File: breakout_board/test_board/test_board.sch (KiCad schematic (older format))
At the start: 12 parts, among them P1 CONN_01X05, P2 CONN_01X02, P3 CONN_01X25, P4 CONN_01X04, P5 CONN_01X02, P6 CONN_01X04

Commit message: pcb: minor changes
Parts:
- added P7: CONN_01X02, symbol CONN_01X02
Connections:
- net GND: now also P7.1 (P1)
- net VDD: now also P7.2 (P2)
- no-connect marks 0 -> 6
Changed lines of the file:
@@
 $EndComp
 $Comp
-L Earth #PWR4
+L Earth #PWR01
 U 1 1 56ED4F6D
 P 6700 2650
-F 0 "#PWR4" H 6700 2400 50  0001 C CNN
+F 0 "#PWR01" H 6700 2400 50  0001 C CNN
 F 1 "Earth" H 6700 2500 50  0001 C CNN
 F 2 "" H 6700 2650 50  0000 C CNN
@@
 $EndComp
 $Comp
-L Earth #PWR9
+L Earth #PWR02
 U 1 1 56ED53FB
-P 7750 5050
-F 0 "#PWR9" H 7750 4800 50  0001 C CNN
-F 1 "Earth" H 7750 4900 50  0001 C CNN
-F 2 "" H 7750 5050 50  0000 C CNN
-F 3 "" H 7750 5050 50  0000 C CNN
-	1    7750 5050
-	0    1    1    0
-$EndComp
-Text Label 8550 5050 2    60   ~ 0
+P 7350 5050
+F 0 "#PWR02" H 7350 4800 50  0001 C CNN
+F 1 "Earth" H 7350 4900 50  0001 C CNN
+F 2 "" H 7350 5050 50  0000 C CNN
+F 3 "" H 7350 5050 50  0000 C CNN
+	1    7350 5050
+	0    1    1    0
+$EndComp
+Text Label 7750 5050 2    60   ~ 0
 ESD
 Text Label 8400 2750 0    60   ~ 0
@@
 	8100 2650 6700 2650
 Wire Wire Line
-	7750 5050 8100 5050
+	7350 5050 8100 5050
 Text Label 8400 3150 0    60   ~ 0
 VDD
@@
 Connection ~ 5950 3350
 $Comp
-L Earth #PWR3
+L Earth #PWR03
 U 1 1 56ED6FD4
 P 5800 3750
-F 0 "#PWR3" H 5800 3500 50  0001 C CNN
+F 0 "#PWR03" H 5800 3500 50  0001 C CNN
 F 1 "Earth" H 5800 3600 50  0001 C CNN
 F 2 "" H 5800 3750 50  0000 C CNN
@@
 	8100 3950 7750 3950
 $Comp
-L GND #PWR7
+L GND #PWR04
 U 1 1 56ED8B2B
 P 7750 3950
-F 0 "#PWR7" H 7750 3700 50  0001 C CNN
+F 0 "#PWR04" H 7750 3700 50  0001 C CNN
 F 1 "GND" H 7750 3800 50  0000 C CNN
 F 2 "" H 7750 3950 50  0000 C CNN
@@
 	8100 4850 7750 4850
 $Comp
-L GND #PWR8
+L GND #PWR05
 U 1 1 56ED8D65
 P 7750 4850
-F 0 "#PWR8" H 7750 4600 50  0001 C CNN
+F 0 "#PWR05" H 7750 4600 50  0001 C CNN
 F 1 "GND" H 7750 4700 50  0000 C CNN
 F 2 "" H 7750 4850 50  0000 C CNN
@@
 SDA
 $Comp
-L GND #PWR6
+L GND #PWR06
 U 1 1 56ED96BD
 P 7750 3700
-F 0 "#PWR6" H 7750 3450 50  0001 C CNN
+F 0 "#PWR06" H 7750 3450 50  0001 C CNN
 F 1 "GND" H 7750 3550 50  0000 C CNN
 F 2 "" H 7750 3700 50  0000 C CNN
@@
 	7000 3350 8100 3350
 $Comp
-L Earth #PWR5
+L Earth #PWR07
 U 1 1 56ED9873
 P 7000 3750
-F 0 "#PWR5" H 7000 3500 50  0001 C CNN
+F 0 "#PWR07" H 7000 3500 50  0001 C CNN
 F 1 "Earth" H 7000 3600 50  0001 C CNN
 F 2 "" H 7000 3750 50  0000 C CNN
@@
 	5750 3350 6350 3350
 $Comp
-L VDD #PWR2
+L VDD #PWR08
 U 1 1 56ED9A6A
 P 5750 3350
-F 0 "#PWR2" H 5750 3200 50  0001 C CNN
+F 0 "#PWR08" H 5750 3200 50  0001 C CNN
 F 1 "VDD" H 5750 3500 50  0000 C CNN
 F 2 "" H 5750 3350 50  0000 C CNN
@@
 	6250 3250 5350 3250
 $Comp
-L Earth #PWR1
+L Earth #PWR09
 U 1 1 56EDA160
 P 4750 3050
-F 0 "#PWR1" H 4750 2800 50  0001 C CNN
+F 0 "#PWR09" H 4750 2800 50  0001 C CNN
 F 1 "Earth" H 4750 2900 50  0001 C CNN
 F 2 "" H 4750 3050 50  0000 C CNN
@@
 Text Label 6650 5600 0    60   ~ 0
 YU
+$Comp
+L CONN_01X02 P7
+U 1 1 56EDDFD4
+P 4100 3600
+F 0 "P7" H 4100 3750 50  0000 C CNN
+F 1 "CONN_01X02" V 4200 3600 50  0000 C CNN
+F 2 "" H 4100 3600 50  0000 C CNN
+F 3 "" H 4100 3600 50  0000 C CNN
+	1    4100 3600
+	-1   0    0    1
+$EndComp
+Wire Wire Line
+	4300 3550 4550 3550
+Wire Wire Line
+	4300 3650 4550 3650
+Text Label 4550 3550 0    60   ~ 0
+VDD
+Text Label 4550 3650 0    60   ~ 0
+GND
+NoConn ~ 8100 4050
+NoConn ~ 8100 4150
+NoConn ~ 8100 4250
+NoConn ~ 8100 4350
+NoConn ~ 8100 4450
+NoConn ~ 8100 4550
+$Comp
+L PWR_FLAG #FLG010
+U 1 1 56EDE7CF
+P 5650 4350
+F 0 "#FLG010" H 5650 4445 50  0001 C CNN
+F 1 "PWR_FLAG" H 5650 4530 50  0000 C CNN
+F 2 "" H 5650 4350 50  0000 C CNN
+F 3 "" H 5650 4350 50  0000 C CNN
+	1    5650 4350
+	1    0    0    -1
+$EndComp
+$Comp
+L PWR_FLAG #FLG011
+U 1 1 56EDE7FD
+P 6250 4350
+F 0 "#FLG011" H 6250 4445 50  0001 C CNN
+F 1 "PWR_FLAG" H 6250 4530 50  0000 C CNN
+F 2 "" H 6250 4350 50  0000 C CNN
+F 3 "" H 6250 4350 50  0000 C CNN
+	1    6250 4350
+	1    0    0    -1
+$EndComp
+$Comp
+L GND #PWR012
+U 1 1 56EDE82B
+P 6250 4350
+F 0 "#PWR012" H 6250 4100 50  0001 C CNN
+F 1 "GND" H 6250 4200 50  0000 C CNN
+F 2 "" H 6250 4350 50  0000 C CNN
+F 3 "" H 6250 4350 50  0000 C CNN
+	1    6250 4350
+	1    0    0    -1
+$EndComp
+$Comp
+L VDD #PWR013
+U 1 1 56EDE859
+P 5650 4350
+F 0 "#PWR013" H 5650 4200 50  0001 C CNN
+F 1 "VDD" H 5650 4500 50  0000 C CNN
+F 2 "" H 5650 4350 50  0000 C CNN
+F 3 "" H 5650 4350 50  0000 C CNN
+	1    5650 4350
+	-1   0    0    1
+$EndComp
 $EndSCHEMATC

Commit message: pcb: added footprint for the capacitors
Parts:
- C1: footprint (none) -> Capacitors_SMD:C_0603_HandSoldering
- C2, C3, C4, C5: footprint (none) -> Capacitors_SMD:C_1206_HandSoldering
- C6: footprint (none) -> Capacitors_SMD:C_0402
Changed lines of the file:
@@
 LIBS:contrib
 LIBS:valves
+LIBS:test_board-cache
 EELAYER 25 0
 EELAYER END
@@
 F 0 "P3" H 8300 5150 50  0000 C CNN
 F 1 "CONN_01X25" V 8400 3850 50  0000 C CNN
-F 2 "" H 8300 3850 50  0000 C CNN
+F 2 "" H 8300 3850 50  0001 C CNN
 F 3 "" H 8300 3850 50  0000 C CNN
 	1    8300 3850
@@
 F 0 "P4" H 8300 5700 50  0000 C CNN
 F 1 "CONN_01X04" V 8400 5450 50  0000 C CNN
-F 2 "" H 8300 5450 50  0000 C CNN
+F 2 "" H 8300 5450 50  0001 C CNN
 F 3 "" H 8300 5450 50  0000 C CNN
 	1    8300 5450
@@
 F 0 "P2" H 8250 2350 50  0000 C CNN
 F 1 "CONN_01X02" V 8350 2200 50  0000 C CNN
-F 2 "" H 8250 2200 50  0000 C CNN
+F 2 "" H 8250 2200 50  0001 C CNN
 F 3 "" H 8250 2200 50  0000 C CNN
 	1    8250 2200
@@
 F 0 "P1" H 4100 4600 50  0000 C CNN
 F 1 "CONN_01X05" V 4200 4300 50  0000 C CNN
-F 2 "" H 4100 4300 50  0000 C CNN
+F 2 "" H 4100 4300 50  0001 C CNN
 F 3 "" H 4100 4300 50  0000 C CNN
 	1    4100 4300
@@
 F 0 "C4" H 5975 3100 50  0000 L CNN
 F 1 "1uF" H 5975 2900 50  0000 L CNN
-F 2 "" H 5988 2850 50  0000 C CNN
+F 2 "Capacitors_SMD:C_1206_HandSoldering" H 5988 2850 50  0001 C CNN
 F 3 "" H 5950 3000 50  0000 C CNN
 	1    5950 3000
@@
 F 0 "C5" H 7025 3600 50  0000 L CNN
 F 1 "1uF" H 7025 3400 50  0000 L CNN
-F 2 "" H 7038 3350 50  0000 C CNN
+F 2 "Capacitors_SMD:C_1206_HandSoldering" H 7038 3350 50  0001 C CNN
 F 3 "" H 7000 3500 50  0000 C CNN
 	1    7000 3500
@@
 F 0 "C2" H 5125 2950 50  0000 L CNN
 F 1 "1uF" H 5125 2750 50  0000 L CNN
-F 2 "" H 5138 2700 50  0000 C CNN
+F 2 "Capacitors_SMD:C_1206_HandSoldering" H 5138 2700 50  0001 C CNN
 F 3 "" H 5100 2850 50  0000 C CNN
 	1    5100 2850
@@
 F 0 "C3" H 5225 3350 50  0000 L CNN
 F 1 "1uF" H 5225 3150 50  0000 L CNN
-F 2 "" H 5238 3100 50  0000 C CNN
+F 2 "Capacitors_SMD:C_1206_HandSoldering" H 5238 3100 50  0001 C CNN
 F 3 "" H 5200 3250 50  0000 C CNN
 	1    5200 3250
@@
 F 0 "C1" H 5975 3650 50  0000 L CNN
 F 1 "10uF" H 5975 3450 50  0000 L CNN
-F 2 "" H 5950 3550 50  0000 C CNN
+F 2 "Capacitors_SMD:C_0603_HandSoldering" H 5950 3550 50  0001 C CNN
 F 3 "" H 5950 3550 50  0000 C CNN
 	1    5950 3550
@@
 F 0 "C6" H 6225 3650 50  0000 L CNN
 F 1 "0.1uF" H 6225 3450 50  0000 L CNN
-F 2 "" H 6238 3400 50  0000 C CNN
+F 2 "Capacitors_SMD:C_0402" H 6238 3400 50  0001 C CNN
 F 3 "" H 6200 3550 50  0000 C CNN
 	1    6200 3550
@@
 F 0 "P5" H 4050 2350 50  0000 C CNN
 F 1 "CONN_01X02" V 4150 2200 50  0000 C CNN
-F 2 "" H 4050 2200 50  0000 C CNN
+F 2 "" H 4050 2200 50  0001 C CNN
 F 3 "" H 4050 2200 50  0000 C CNN
 	1    4050 2200
@@
 F 0 "P6" H 4100 5700 50  0000 C CNN
 F 1 "CONN_01X04" V 4200 5450 50  0000 C CNN
-F 2 "" H 4100 5450 50  0000 C CNN
+F 2 "" H 4100 5450 50  0001 C CNN
 F 3 "" H 4100 5450 50  0000 C CNN
 	1    4100 5450
@@
 F 0 "P7" H 4100 3750 50  0000 C CNN
 F 1 "CONN_01X02" V 4200 3600 50  0000 C CNN
-F 2 "" H 4100 3600 50  0000 C CNN
+F 2 "" H 4100 3600 50  0001 C CNN
 F 3 "" H 4100 3600 50  0000 C CNN
 	1    4100 3600

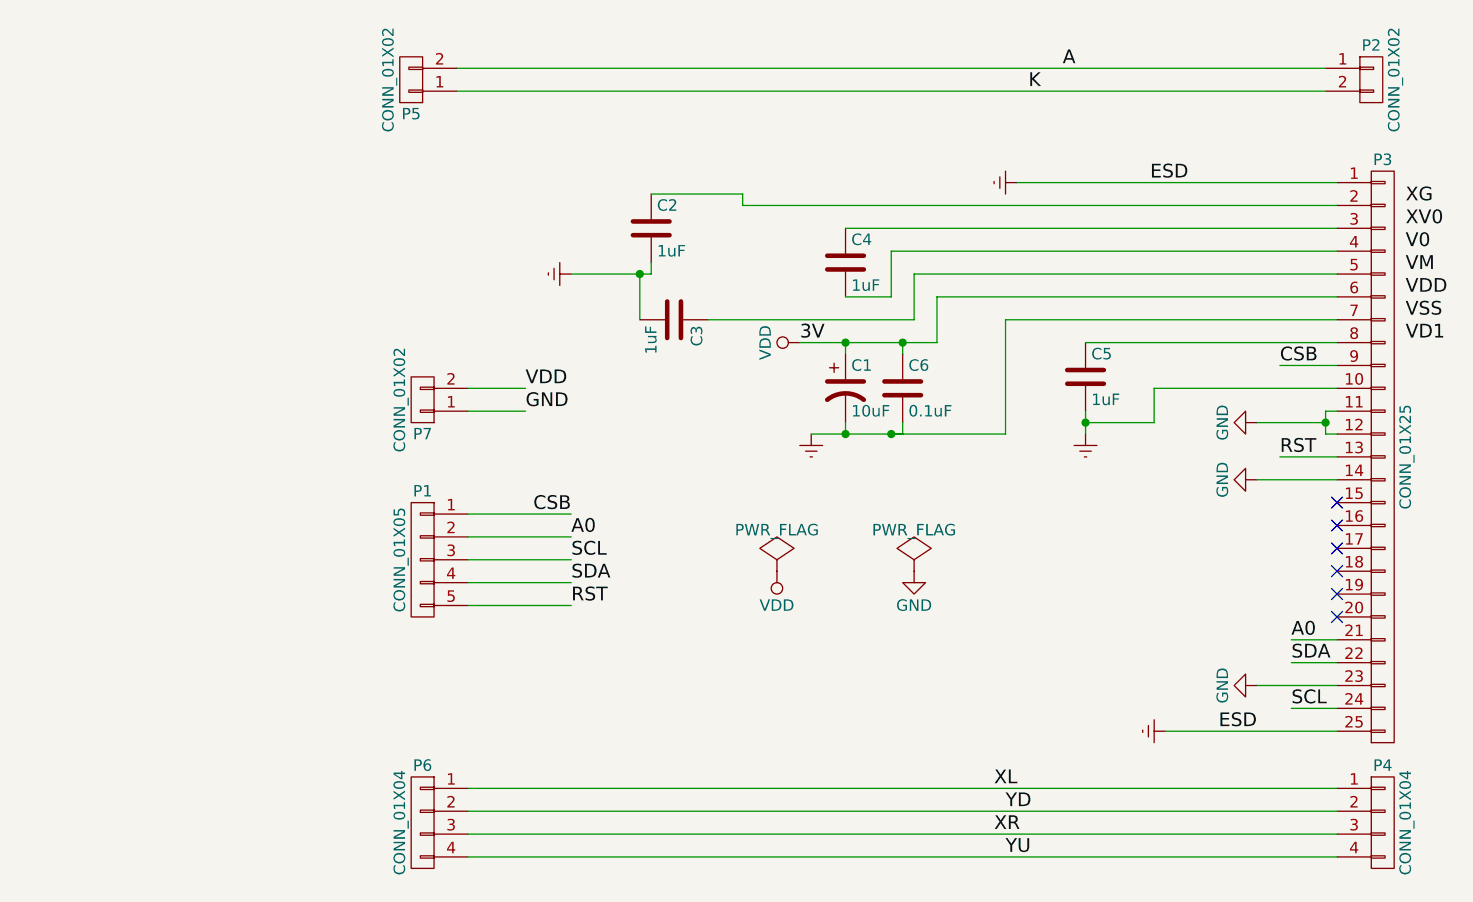
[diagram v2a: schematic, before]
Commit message: pcb: added all the footprints
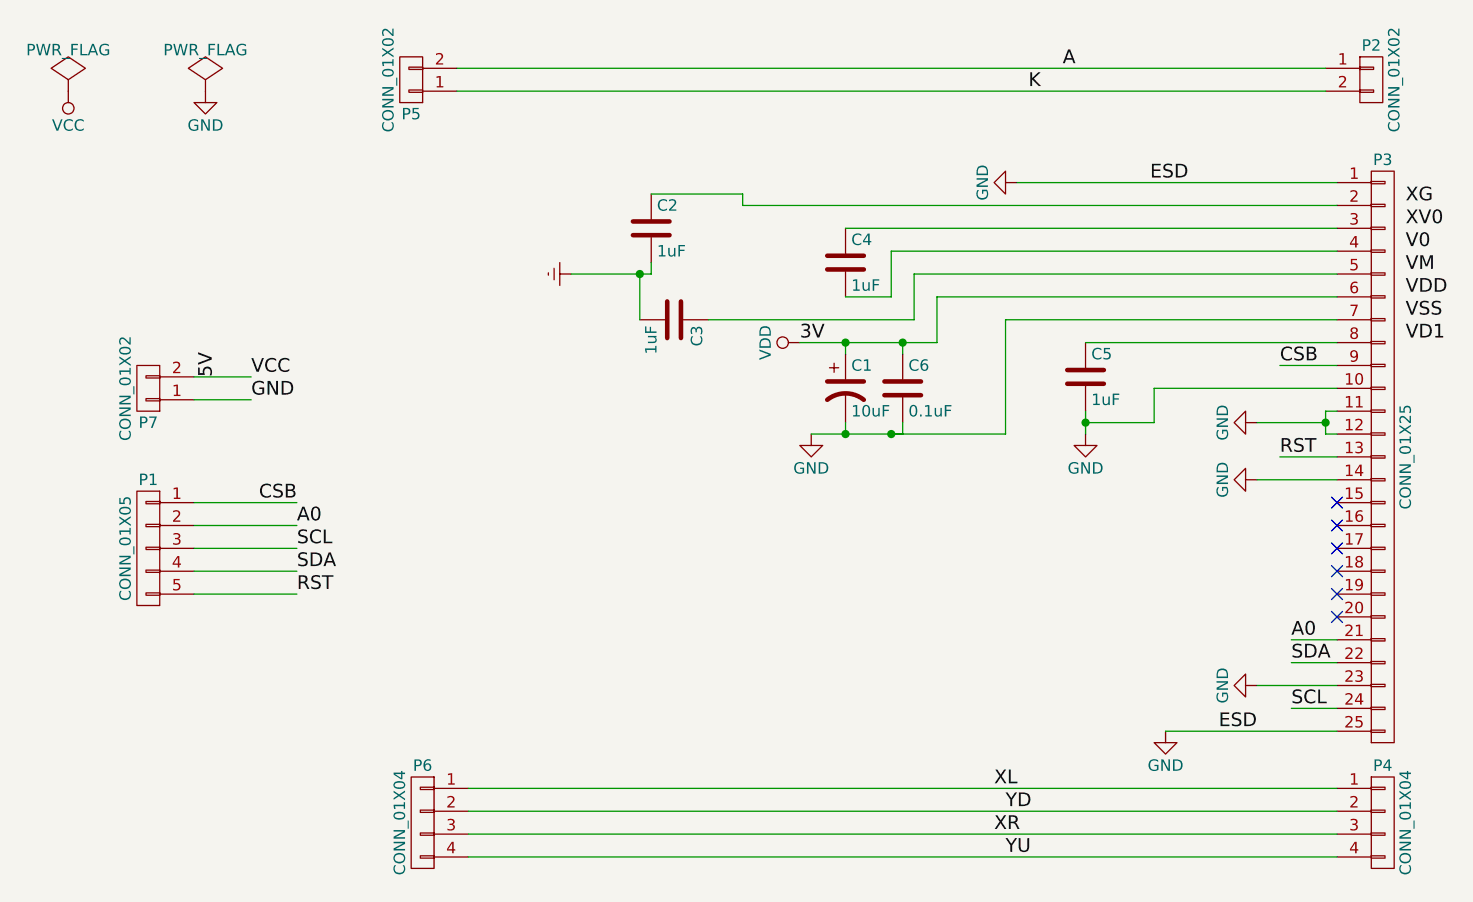
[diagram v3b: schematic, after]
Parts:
- P1: footprint (none) -> Socket_Strips:Socket_Strip_Straight_1x05
- P2, P5, P7: footprint (none) -> MyFootprints:Molex_kk_22_2_2021
- P3: footprint (none) -> MyFootprints:fpc_lcd
- P4: footprint (none) -> MyFootprints:SLW4S-1C7LF
- P6: footprint (none) -> Socket_Strips:Socket_Strip_Straight_1x04
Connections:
- net Earth: no longer C1.2, C5.2, C6.2, P3.1 (P1), P3.10 (P10), P3.25 (P25), P3.7 (P7)
- net GND: now also C1.2, C5.2, C6.2, P3.1 (P1), P3.10 (P10), P3.25 (P25), P3.7 (P7)
- net VDD: no longer P7.2 (P2)
- new net VCC: P7.2 (P2)
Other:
- moved on the sheet: P1, P7
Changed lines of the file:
@@
 F 0 "P3" H 8300 5150 50  0000 C CNN
 F 1 "CONN_01X25" V 8400 3850 50  0000 C CNN
-F 2 "" H 8300 3850 50  0001 C CNN
+F 2 "MyFootprints:fpc_lcd" H 8300 3850 50  0001 C CNN
 F 3 "" H 8300 3850 50  0000 C CNN
 	1    8300 3850
@@
 F 0 "P4" H 8300 5700 50  0000 C CNN
 F 1 "CONN_01X04" V 8400 5450 50  0000 C CNN
-F 2 "" H 8300 5450 50  0001 C CNN
+F 2 "MyFootprints:SLW4S-1C7LF" H 8300 5450 50  0001 C CNN
 F 3 "" H 8300 5450 50  0000 C CNN
 	1    8300 5450
@@
 F 0 "P2" H 8250 2350 50  0000 C CNN
 F 1 "CONN_01X02" V 8350 2200 50  0000 C CNN
-F 2 "" H 8250 2200 50  0001 C CNN
+F 2 "MyFootprints:Molex_kk_22_2_2021" H 8250 2200 50  0001 C CNN
 F 3 "" H 8250 2200 50  0000 C CNN
 	1    8250 2200
@@
 L CONN_01X05 P1
 U 1 1 56ED3F33
-P 4100 4300
-F 0 "P1" H 4100 4600 50  0000 C CNN
-F 1 "CONN_01X05" V 4200 4300 50  0000 C CNN
-F 2 "" H 4100 4300 50  0001 C CNN
-F 3 "" H 4100 4300 50  0000 C CNN
-	1    4100 4300
+P 2900 4250
+F 0 "P1" H 2900 4550 50  0000 C CNN
+F 1 "CONN_01X05" V 3000 4250 50  0000 C CNN
+F 2 "Socket_Strips:Socket_Strip_Straight_1x05" H 2900 4250 50  0001 C CNN
+F 3 "" H 2900 4250 50  0000 C CNN
+	1    2900 4250
 	-1   0    0    -1
 $EndComp
@@
 	1    5950 3550
 	1    0    0    -1
-$EndComp
-$Comp
-L Earth #PWR01
-U 1 1 56ED4F6D
-P 6700 2650
-F 0 "#PWR01" H 6700 2400 50  0001 C CNN
-F 1 "Earth" H 6700 2500 50  0001 C CNN
-F 2 "" H 6700 2650 50  0000 C CNN
-F 3 "" H 6700 2650 50  0000 C CNN
-	1    6700 2650
-	0    1    1    0
-$EndComp
-$Comp
-L Earth #PWR02
-U 1 1 56ED53FB
-P 7350 5050
-F 0 "#PWR02" H 7350 4800 50  0001 C CNN
-F 1 "Earth" H 7350 4900 50  0001 C CNN
-F 2 "" H 7350 5050 50  0000 C CNN
-F 3 "" H 7350 5050 50  0000 C CNN
-	1    7350 5050
-	0    1    1    0
 $EndComp
 Text Label 7750 5050 2    60   ~ 0
@@
 	5950 3400 5950 3350
 Connection ~ 5950 3350
-$Comp
-L Earth #PWR03
-U 1 1 56ED6FD4
-P 5800 3750
-F 0 "#PWR03" H 5800 3500 50  0001 C CNN
-F 1 "Earth" H 5800 3600 50  0001 C CNN
-F 2 "" H 5800 3750 50  0000 C CNN
-F 3 "" H 5800 3750 50  0000 C CNN
-	1    5800 3750
-	1    0    0    -1
-$EndComp
 Wire Wire Line
 	6200 3750 6200 3700
@@
 ESD
 Wire Wire Line
-	4300 4100 4750 4100
-Text Label 4750 4100 2    60   ~ 0
+	3100 4050 3550 4050
+Text Label 3550 4050 2    60   ~ 0
 CSB
 Wire Wire Line
@@
 CSB
 Wire Wire Line
-	4300 4500 4750 4500
-Wire Wire Line
-	4300 4400 4750 4400
-Wire Wire Line
-	4300 4300 4750 4300
-Wire Wire Line
-	4300 4200 4750 4200
-Text Label 4750 4500 0    60   ~ 0
+	3100 4450 3550 4450
+Wire Wire Line
+	3100 4350 3550 4350
+Wire Wire Line
+	3100 4250 3550 4250
+Wire Wire Line
+	3100 4150 3550 4150
+Text Label 3550 4450 0    60   ~ 0
 RST
 Wire Wire Line
@@
 	8100 3950 7750 3950
 $Comp
-L GND #PWR04
+L GND #PWR01
 U 1 1 56ED8B2B
 P 7750 3950
-F 0 "#PWR04" H 7750 3700 50  0001 C CNN
+F 0 "#PWR01" H 7750 3700 50  0001 C CNN
 F 1 "GND" H 7750 3800 50  0000 C CNN
 F 2 "" H 7750 3950 50  0000 C CNN
@@
 	8100 4850 7750 4850
 $Comp
-L GND #PWR05
+L GND #PWR02
 U 1 1 56ED8D65
 P 7750 4850
-F 0 "#PWR05" H 7750 4600 50  0001 C CNN
+F 0 "#PWR02" H 7750 4600 50  0001 C CNN
 F 1 "GND" H 7750 4700 50  0000 C CNN
 F 2 "" H 7750 4850 50  0000 C CNN
@@
 Text Label 7900 4950 0    60   ~ 0
 SCL
-Text Label 4750 4200 0    60   ~ 0
+Text Label 3550 4150 0    60   ~ 0
 A0
-Text Label 4750 4300 0    60   ~ 0
+Text Label 3550 4250 0    60   ~ 0
 SCL
-Text Label 4750 4400 0    60   ~ 0
+Text Label 3550 4350 0    60   ~ 0
 SDA
 $Comp
-L GND #PWR06
+L GND #PWR03
 U 1 1 56ED96BD
 P 7750 3700
-F 0 "#PWR06" H 7750 3450 50  0001 C CNN
+F 0 "#PWR03" H 7750 3450 50  0001 C CNN
 F 1 "GND" H 7750 3550 50  0000 C CNN
 F 2 "" H 7750 3700 50  0000 C CNN
@@
 Wire Wire Line
 	7000 3350 8100 3350
-$Comp
-L Earth #PWR07
-U 1 1 56ED9873
-P 7000 3750
-F 0 "#PWR07" H 7000 3500 50  0001 C CNN
-F 1 "Earth" H 7000 3600 50  0001 C CNN
-F 2 "" H 7000 3750 50  0000 C CNN
-F 3 "" H 7000 3750 50  0000 C CNN
-	1    7000 3750
-	1    0    0    -1
-$EndComp
 Wire Wire Line
 	7000 3650 7000 3750
@@
 	5750 3350 6350 3350
 $Comp
-L VDD #PWR08
+L VDD #PWR04
 U 1 1 56ED9A6A
 P 5750 3350
-F 0 "#PWR08" H 5750 3200 50  0001 C CNN
+F 0 "#PWR04" H 5750 3200 50  0001 C CNN
 F 1 "VDD" H 5750 3500 50  0000 C CNN
 F 2 "" H 5750 3350 50  0000 C CNN
@@
 	6250 3250 5350 3250
 $Comp
-L Earth #PWR09
+L Earth #PWR05
 U 1 1 56EDA160
 P 4750 3050
-F 0 "#PWR09" H 4750 2800 50  0001 C CNN
+F 0 "#PWR05" H 4750 2800 50  0001 C CNN
 F 1 "Earth" H 4750 2900 50  0001 C CNN
 F 2 "" H 4750 3050 50  0000 C CNN
@@
 F 0 "P5" H 4050 2350 50  0000 C CNN
 F 1 "CONN_01X02" V 4150 2200 50  0000 C CNN
-F 2 "" H 4050 2200 50  0001 C CNN
+F 2 "MyFootprints:Molex_kk_22_2_2021" H 4050 2200 50  0001 C CNN
 F 3 "" H 4050 2200 50  0000 C CNN
 	1    4050 2200
@@
 F 0 "P6" H 4100 5700 50  0000 C CNN
 F 1 "CONN_01X04" V 4200 5450 50  0000 C CNN
-F 2 "" H 4100 5450 50  0001 C CNN
+F 2 "Socket_Strips:Socket_Strip_Straight_1x04" H 4100 5450 50  0001 C CNN
 F 3 "" H 4100 5450 50  0000 C CNN
 	1    4100 5450
@@
 L CONN_01X02 P7
 U 1 1 56EDDFD4
-P 4100 3600
-F 0 "P7" H 4100 3750 50  0000 C CNN
-F 1 "CONN_01X02" V 4200 3600 50  0000 C CNN
-F 2 "" H 4100 3600 50  0001 C CNN
-F 3 "" H 4100 3600 50  0000 C CNN
-	1    4100 3600
+P 2900 3550
+F 0 "P7" H 2900 3700 50  0000 C CNN
+F 1 "CONN_01X02" V 3000 3550 50  0000 C CNN
+F 2 "MyFootprints:Molex_kk_22_2_2021" H 2900 3550 50  0001 C CNN
+F 3 "" H 2900 3550 50  0000 C CNN
+	1    2900 3550
 	-1   0    0    1
 $EndComp
 Wire Wire Line
-	4300 3550 4550 3550
-Wire Wire Line
-	4300 3650 4550 3650
-Text Label 4550 3550 0    60   ~ 0
-VDD
-Text Label 4550 3650 0    60   ~ 0
+	3100 3500 3350 3500
+Wire Wire Line
+	3100 3600 3350 3600
+Text Label 3350 3500 0    60   ~ 0
+VCC
+Text Label 3350 3600 0    60   ~ 0
 GND
 NoConn ~ 8100 4050
@@
 NoConn ~ 8100 4550
 $Comp
-L PWR_FLAG #FLG010
+L PWR_FLAG #FLG06
 U 1 1 56EDE7CF
-P 5650 4350
-F 0 "#FLG010" H 5650 4445 50  0001 C CNN
-F 1 "PWR_FLAG" H 5650 4530 50  0000 C CNN
-F 2 "" H 5650 4350 50  0000 C CNN
-F 3 "" H 5650 4350 50  0000 C CNN
-	1    5650 4350
-	1    0    0    -1
-$EndComp
-$Comp
-L PWR_FLAG #FLG011
+P 2550 2250
+F 0 "#FLG06" H 2550 2345 50  0001 C CNN
+F 1 "PWR_FLAG" H 2550 2430 50  0000 C CNN
+F 2 "" H 2550 2250 50  0000 C CNN
+F 3 "" H 2550 2250 50  0000 C CNN
+	1    2550 2250
+	1    0    0    -1
+$EndComp
+$Comp
+L PWR_FLAG #FLG07
 U 1 1 56EDE7FD
-P 6250 4350
-F 0 "#FLG011" H 6250 4445 50  0001 C CNN
-F 1 "PWR_FLAG" H 6250 4530 50  0000 C CNN
-F 2 "" H 6250 4350 50  0000 C CNN
-F 3 "" H 6250 4350 50  0000 C CNN
-	1    6250 4350
+P 3150 2250
+F 0 "#FLG07" H 3150 2345 50  0001 C CNN
+F 1 "PWR_FLAG" H 3150 2430 50  0000 C CNN
+F 2 "" H 3150 2250 50  0000 C CNN
+F 3 "" H 3150 2250 50  0000 C CNN
+	1    3150 2250
+	1    0    0    -1
+$EndComp
+$Comp
+L GND #PWR08
+U 1 1 56EDE82B
+P 3150 2250
+F 0 "#PWR08" H 3150 2000 50  0001 C CNN
+F 1 "GND" H 3150 2100 50  0000 C CNN
+F 2 "" H 3150 2250 50  0000 C CNN
+F 3 "" H 3150 2250 50  0000 C CNN
+	1    3150 2250
+	1    0    0    -1
+$EndComp
+Text Label 3200 3500 1    60   ~ 0
+5V
+$Comp
+L VCC #PWR09
+U 1 1 56EDC101
+P 2550 2250
+F 0 "#PWR09" H 2550 2100 50  0001 C CNN
+F 1 "VCC" H 2550 2400 50  0000 C CNN
+F 2 "" H 2550 2250 50  0000 C CNN
+F 3 "" H 2550 2250 50  0000 C CNN
+	1    2550 2250
+	-1   0    0    1
+$EndComp
+$Comp
+L GND #PWR010
+U 1 1 56EDC13D
+P 7350 5050
+F 0 "#PWR010" H 7350 4800 50  0001 C CNN
+F 1 "GND" H 7350 4900 50  0000 C CNN
+F 2 "" H 7350 5050 50  0000 C CNN
+F 3 "" H 7350 5050 50  0000 C CNN
+	1    7350 5050
+	1    0    0    -1
+$EndComp
+$Comp
+L GND #PWR011
+U 1 1 56EDC179
+P 7000 3750
+F 0 "#PWR011" H 7000 3500 50  0001 C CNN
+F 1 "GND" H 7000 3600 50  0000 C CNN
+F 2 "" H 7000 3750 50  0000 C CNN
+F 3 "" H 7000 3750 50  0000 C CNN
+	1    7000 3750
 	1    0    0    -1
 $EndComp
 $Comp
 L GND #PWR012
-U 1 1 56EDE82B
-P 6250 4350
-F 0 "#PWR012" H 6250 4100 50  0001 C CNN
-F 1 "GND" H 6250 4200 50  0000 C CNN
-F 2 "" H 6250 4350 50  0000 C CNN
-F 3 "" H 6250 4350 50  0000 C CNN
-	1    6250 4350
-	1    0    0    -1
-$EndComp
-$Comp
-L VDD #PWR013
-U 1 1 56EDE859
-P 5650 4350
-F 0 "#PWR013" H 5650 4200 50  0001 C CNN
-F 1 "VDD" H 5650 4500 50  0000 C CNN
-F 2 "" H 5650 4350 50  0000 C CNN
-F 3 "" H 5650 4350 50  0000 C CNN
-	1    5650 4350
-	-1   0    0    1
+U 1 1 56EDC1B5
+P 5800 3750
+F 0 "#PWR012" H 5800 3500 50  0001 C CNN
+F 1 "GND" H 5800 3600 50  0000 C CNN
+F 2 "" H 5800 3750 50  0000 C CNN
+F 3 "" H 5800 3750 50  0000 C CNN
+	1    5800 3750
+	1    0    0    -1
+$EndComp
+$Comp
+L GND #PWR013
+U 1 1 56EDC8B2
+P 6700 2650
+F 0 "#PWR013" H 6700 2400 50  0001 C CNN
+F 1 "GND" H 6700 2500 50  0000 C CNN
+F 2 "" H 6700 2650 50  0000 C CNN
+F 3 "" H 6700 2650 50  0000 C CNN
+	1    6700 2650
+	0    1    1    0
 $EndComp
 $EndSCHEMATC
